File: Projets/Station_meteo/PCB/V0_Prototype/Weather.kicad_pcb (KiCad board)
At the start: 2 copper layers, 94.4 x 77 mm, 161 parts, among them J1 SolderJumper_2_Bridged, J10 SolderJumper_2_Bridged, J11 SolderJumper_2_Bridged, J12 SolderJumper_2_Bridged, J13 SolderJumper_2_Bridged, J14 SolderJumper_2_Bridged, J15 SolderJumper_2_Bridged, J16 SolderJumper_2_Bridged, J17 SolderJumper_2_Bridged, J18 SolderJumper_2_Bridged, J19 SolderJumper_2_Bridged, J2 SolderJumper_2_Bridged, J20 SolderJumper_2_Bridged, J21 SolderJumper_2_Bridged, J22 SolderJumper_2_Bridged, J23 SolderJumper_2_Bridged, J24 Anemometer, J25 KF128-2.54_2P, J26 Panel, J27 132415, J28 SolderJumper_2_Bridged, J29 USB_C_Receptacle_USB2.0_16P, J3 SolderJumper_2_Bridged, J30 KF128-2.54_2P, J31 Wind_Direction, J32 Water_Level, J33 Screw_Terminal_01x04, J34 SolderJumper_2_Bridged, J4 SolderJumper_2_Bridged, J5 SolderJumper_2_Bridged, J6 SolderJumper_2_Bridged, J7 SolderJumper_2_Bridged, J8 SolderJumper_2_Bridged, J9 SolderJumper_2_Bridged, Q1 CJ3401, Q2 2N7002H, Q3 CJ3401, Q4 2N7002H, Q5 CJ3401, Q6 2N7002H, SW1 PB_SMD_12V_50MA_6MM_6MM, SW2 PB_SMD_12V_50MA_6MM_6MM, T1 TP, T10 TP, T11 TP, T14 TP, T15 TP, T16 TP, T17 TP, T18 TP, T19 TP, T2 TP, T20 TP, T3 TP, T4 TP, T5 TP, T6 TP, T7 TP, T8 TP, T9 TP, U1 ATMEGA-328P, U10 USBLC6-2P6, U11 CH340G, U12 AMS1117-3.3, U13 DS3231M, U2 LM358DR, U3 74HC123D, U6 LM317_SOT-223, U7 BL8530, U8 NRF24L01, U9 NEO-M8M, Y1 16MHz, Y2 16MHz, Y3 12MHz

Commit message: Update PCB
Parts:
- removed C31: 100nF, Capacitor_SMD:C_0603_1608Metric
- removed C32, C7: 22pF, Capacitor_SMD:C_0603_1608Metric
- removed T3, T6, T7, T8: TP, TestPoint:TestPoint_Pad_D1.0mm
- removed Y1: 16MHz, Crystal:Crystal_SMD_HC49-SD
- added H1: MountingHole_Pad, MountingHole:MountingHole_3.2mm_M3, F.Cu at (117.9, 64.8)
- added H2: MountingHole_Pad, MountingHole:MountingHole_3.2mm_M3, F.Cu at (45.7, 64.8)
- added H3: MountingHole_Pad, MountingHole:MountingHole_3.2mm_M3, F.Cu at (45.7, 136.7)
- added H4: MountingHole_Pad, MountingHole:MountingHole_3.2mm_M3, F.Cu at (117.9, 136.7)
- added J35: Screw_Terminal_01x03, Connector_Phoenix_MSTB:PhoenixContact_MSTBA_2,5_3-G-5,08_1x03_P5.08mm_Horizontal, F.Cu at (75.2, 128.1)
- added J36: Conn_01x01_Pin, Connector_PinHeader_2.54mm:PinHeader_1x01_P2.54mm_Vertical, F.Cu at (66.3, 86.3)
- added J37: Conn_01x01_Pin, Connector_PinHeader_2.54mm:PinHeader_1x01_P2.54mm_Vertical, F.Cu at (66.4, 89.0)
- added J38: Conn_01x01_Pin, Connector_PinHeader_2.54mm:PinHeader_1x01_P2.54mm_Vertical, F.Cu at (71.8, 86.3)
- added J39: SolderJumper_2_Bridged, Jumper:SolderJumper-2_P1.3mm_Bridged_Pad1.0x1.5mm, F.Cu at (95.9, 93.2)
- added R21: 100k, Resistor_SMD:R_0603_1608Metric, F.Cu at (91.1, 124.7)
- C3, C4, C5, C6, D2, R3, R4, R5, T10, T11, T9, U13, U2, U3: moved to F.Cu
- J31: value Wind_Direction -> Conn_01x01_Pin; footprint Connector_Phoenix_MSTB:PhoenixContact_MSTBA_2,5_2-G-5,08_1x02_P5.08mm_Horizontal -> Connector_PinHeader_2.54mm:PinHeader_1x01_P2.54mm_Vertical
- moved J31 42.5 mm to (69.1, 86.3)
- moved C22 26.9 mm to (133.1, 111.9)
- moved R37 26.4 mm to (104.1, 100.2), turned to 180 degrees
- moved L11 24.3 mm to (134.2, 114.4), turned to 90 degrees
- moved U3 23.4 mm to (108.3, 118.6), turned to -90 degrees
- moved Q3 23.0 mm to (104.0, 108.9), turned to -90 degrees
- moved U13 22.6 mm to (88.7, 115.6), turned to 0 degrees
- moved Q4 21.5 mm to (104.0, 103.1), turned to -90 degrees
- moved C19 20.5 mm to (125.6, 109.3), turned to -90 degrees
- moved T18 20.2 mm to (113.9, 90.9)
- moved R36 20.2 mm to (104.0, 106.0), turned to 180 degrees
- moved L10 18.8 mm to (134.9, 117.2)
- moved L1 18.3 mm to (132.3, 115.5), turned to 90 degrees
- moved T11 15.8 mm to (101.8, 113.5), turned to 0 degrees
- moved C20 15.5 mm to (127.7, 117.2)
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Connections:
- net /Power/Vcap renamed Net-(D5-K)
- net /RTC/+3.3V renamed /Interfaces/+3.3V
- J11 pad 2: /MCU/PC2-A2 -> /Interfaces/Direction
- J18 pad 2: /MCU/PD2-D2-(INT0) -> /Interfaces/Water_Level
- J30 pad 2: /MCU/PB2-D10~ -> /MCU/PD3-D3-(INT1)~
- J31 pad 1: unconnected-(J31-Pin_1-Pad1) -> /MCU/MOSI
- J32 pad 1: unconnected-(J32-Pin_1-Pad1) -> /Interfaces/Water_Level
- J32 pad 2: unconnected-(J32-Pin_2-Pad2) -> GND
- L7 pad 2: /+3.3V_MCU -> /MCU/+VCC
- R33 pad 1: /User_Buttons/VCC -> /+3.3V_MCU
- R33 pad 2: /MCU/PB2-D10~ -> /MCU/PD3-D3-(INT1)~
- SW2 pad 2: /MCU/PB2-D10~ -> /MCU/PD3-D3-(INT1)~
- T9 pad 1: /WIND/Simulation -> /MCU/PB1-D9~
- U3 pad 1: /WIND/Simulation -> /MCU/PB1-D9~
- U8 pad 10: /NRF24/XTAL1/XTAl_1 -> /NRF24/XTAl_1
- U8 pad 9: /NRF24/XTAL1/XTAl_2 -> /NRF24/XTAl_2
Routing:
- net /Interfaces/+3.3V: track 0.00 -> 118.1 mm, vias 0 -> 4
- net /MCU/+VCC: track 15.9 -> 66.1 mm, vias 0 -> 6
- net /NRF24/+3.3V: track 2.39 -> 34.6 mm, vias 0 -> 2
- net /RESET: track 13.1 -> 42.5 mm, vias 0 -> 2
- net /MCU/PD3-D3-(INT1)~: track 0.00 -> 29.3 mm
- net /MCU/PB2-D10~: track 27.6 -> 3.91 mm
- net /Programming/D-: track 20.3 -> 0.47 mm, vias 2 -> 0
- net Net-(J24-Pin_2): track 0.00 -> 18.3 mm, vias 0 -> 1
- net /Programming/D+: track 17.8 -> 0.51 mm, vias 2 -> 0
- net /GNSS/+3.3V: track 14.1 -> 29.6 mm
- net Net-(U11-XI): track 12.2 -> 0.00 mm
- net /NRF24/XTAL1/XTAl_1: track 12.0 -> 0.00 mm
- net /NRF24/XTAL1/XTAl_2: track 11.1 -> 0.00 mm
- net Net-(U3A-Q): track 0.00 -> 10.6 mm
- net Net-(U2B-+): track 0.00 -> 10.6 mm
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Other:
- board size 94.4 x 77 mm -> 103.1 x 79.5 mm
- board text added: "${REFERENCE}"
- board text added: "GND"
- board text added: "RTC"
- board text added: "SOLAR_PANEL"
- board text added: "V+"

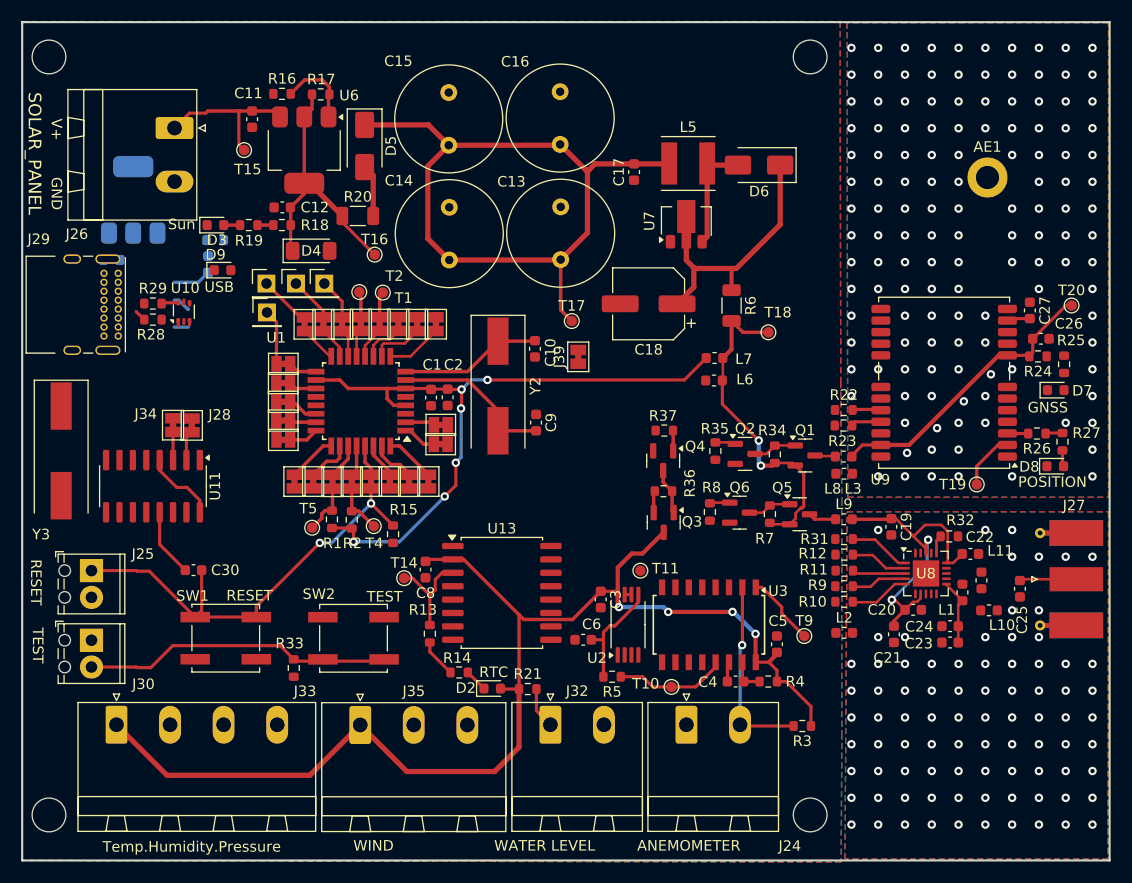
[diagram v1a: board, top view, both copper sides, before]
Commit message: Add V1 THT version
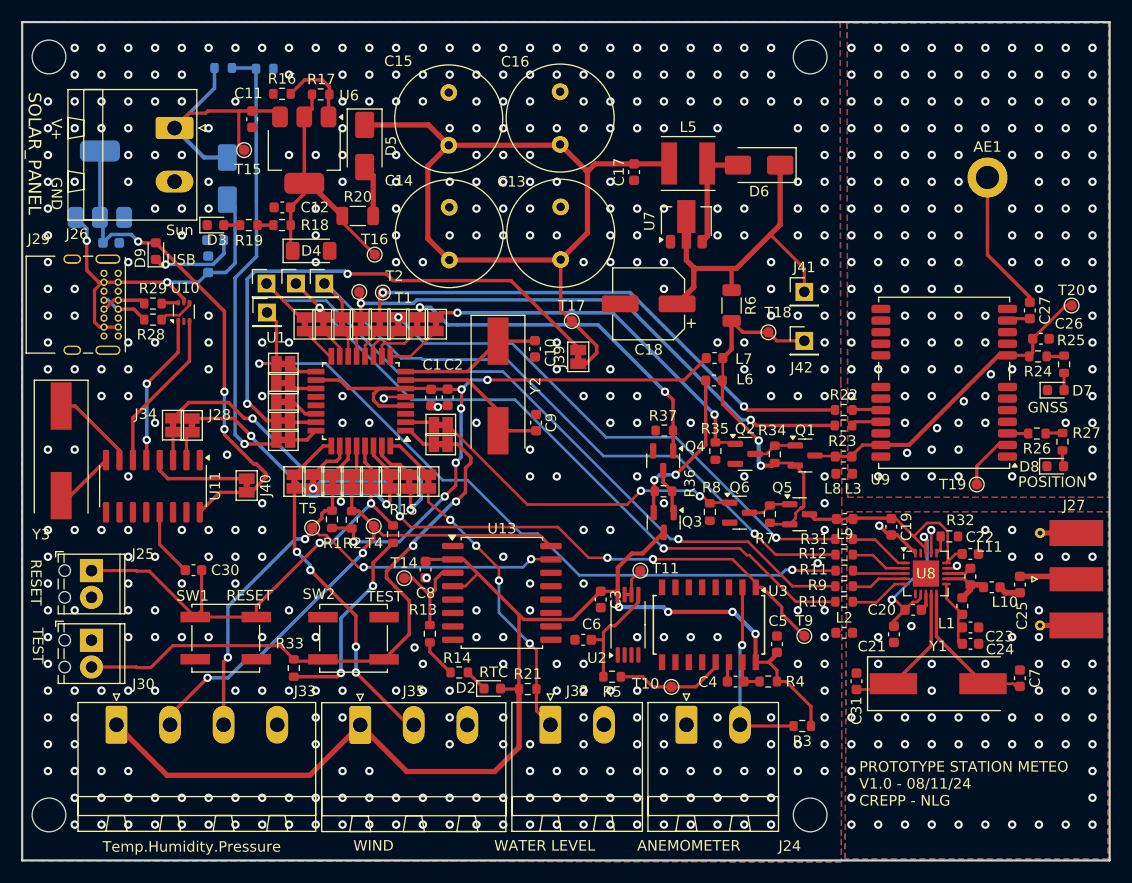
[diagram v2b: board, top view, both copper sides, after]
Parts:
- added C31: 22pF, Capacitor_SMD:C_0603_1608Metric, F.Cu at (122.3, 124.0)
- added C7: 22pF, Capacitor_SMD:C_0603_1608Metric, F.Cu at (137.8, 123.7)
- added D1: SS24, Diode_SMD:D_SMA, B.Cu at (62.6, 76.3)
- added J40: SolderJumper_2_Bridged, Jumper:SolderJumper-2_P1.3mm_Bridged_Pad1.0x1.5mm, F.Cu at (64.5, 105.4)
- added J41: Conn_01x01_Pin, Connector_PinHeader_2.54mm:PinHeader_1x01_P2.54mm_Vertical, F.Cu at (117.3, 87.0)
- added J42: Conn_01x01_Pin, Connector_PinHeader_2.54mm:PinHeader_1x01_P2.54mm_Vertical, F.Cu at (117.3, 91.7)
- added R38: 100k, Resistor_SMD:R_0603_1608Metric, B.Cu at (62.2, 65.8)
- added R39: 100k, Resistor_SMD:R_0603_1608Metric, B.Cu at (66.2, 65.9)
- added Y1: 16MHz, Crystal:Crystal_SMD_HC49-SD, F.Cu at (130.0, 124.2)
- moved D9 6.58 mm to (55.9, 83.2), turned to 90 degrees
- moved U12 3.50 mm to (50.5, 76.8)
- moved C24 2.56 mm to (133.1, 120.4), turned to 0 degrees
- moved C23 2.40 mm to (133.1, 118.9), turned to 0 degrees
- moved L10 2.20 mm to (135.1, 115.1)
- moved C29 1.62 mm to (51.6, 82.4)
- moved L1 1.29 mm to (132.3, 116.8)
- moved L11 1.12 mm to (133.1, 114.0)
- moved C25 0.39 mm to (137.8, 114.8)
- moved L9 0.08 mm to (121.2, 108.6), turned to 180 degrees
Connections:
- net /Programming/RX renamed Net-(J28-A)
- net /Programming/TX renamed Net-(J34-A)
- net /Programming/VBus renamed /+5V_USB
- J16 pad 2: /MCU/TX -> /MCU/RX
- J17 pad 2: /MCU/RX -> /MCU/TX
- J20 pad 2: /MCU/PD4-D4 -> /Enable_RF
- J22 pad 2: /MCU/PD6-D6~ -> /Enable_Sensors
- J23 pad 2: /MCU/PD5-D5~ -> /Enable_GNSS
- J28 pad 2: unconnected-(J28-B-Pad2) -> /MCU/RX
- J33 pad 2: /Temperature/SCL -> /MCU/SCL
- J33 pad 3: /Temperature/SDA -> /MCU/SDA
- J34 pad 2: unconnected-(J34-B-Pad2) -> /MCU/TX
- J4 pad 2: /MCU/PB1-D9~ -> /GNSS/GNSS_RX
- L6 pad 2: unconnected-(L6-Pad2) -> /Power/+3.3V_Sensors
- R10 pad 1: /NRF24/MISO -> /MCU/MOSI
- R11 pad 1: /NRF24/SCK -> /MCU/CLK
- R12 pad 1: /NRF24/CSN -> /MCU/PB2-D10~
- R22 pad 1: /GNSS/GNSS_TX -> /MCU/PB0
- R31 pad 1: /NRF24/CE -> /MCU/PD7-D7
- R9 pad 1: /NRF24/MOSI -> /MCU/MISO
- T2 pad 1: /MCU/PB1-D9~ -> /GNSS/GNSS_RX
- T9 pad 1: /MCU/PB1-D9~ -> /MCU/PC3-A3
- U11 pad 1: unconnected-(U11-GND-Pad1) -> GND
- U11 pad 4: /Programming/+3.3V -> Net-(J40-A)
- U13 pad 15: /RTC/SDA -> /MCU/SDA
- U13 pad 16: /RTC/SCL -> /MCU/SCL
- U13 pad 4: unconnected-(U13-~{RST}-Pad4) -> /Interfaces/+3.3V
- U3 pad 1: /MCU/PB1-D9~ -> /MCU/PC3-A3
- U8 pad 10: /NRF24/XTAl_1 -> /NRF24/XTAL1/XTAl_1
- U8 pad 9: /NRF24/XTAl_2 -> /NRF24/XTAL1/XTAl_2
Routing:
- net /MCU/MISO: track 4.95 -> 70.8 mm, vias 0 -> 1
- net /MCU/CLK: track 5.24 -> 70.1 mm, vias 0 -> 2
- net /MCU/MOSI: track 4.28 -> 64.7 mm, vias 0 -> 2
- net /MCU/PB2-D10~: track 3.91 -> 63.0 mm, vias 0 -> 1
- net /MCU/PC3-A3: track 0.00 -> 54.7 mm, vias 0 -> 4
- net /GNSS/GNSS_RX: track 0.00 -> 52.5 mm, vias 0 -> 2
- net /MCU/PC0-A0: track 0.00 -> 50.2 mm, vias 0 -> 2
- net /MCU/PD7-D7: track 0.00 -> 50.2 mm, vias 0 -> 2
- net /MCU/PB0: track 2.46 -> 50.0 mm, vias 0 -> 2
- net /MCU/SDA: track 4.89 -> 52.1 mm, vias 0 -> 4
- net /MCU/SCL: track 4.82 -> 50.9 mm, vias 0 -> 2
- net /MCU/PC1-A1: track 0.00 -> 42.3 mm, vias 0 -> 1
- net /Programming/+3.3V: track 7.10 -> 48.9 mm, vias 0 -> 3
- net /Enable_GNSS: track 1.94 -> 35.2 mm, vias 0 -> 2
- net /MCU/TX: track 0.00 -> 32.4 mm, vias 0 -> 2
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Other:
- board text added: "PCB3D_BR_BOARD"
- board text added: "PCB3D_TL_BOARD"
- board text added: "PROTOTYPE STATION METEO V1.0 - 08/11/24 CREPP - NLG"
- board text removed: "${REFERENCE}"
